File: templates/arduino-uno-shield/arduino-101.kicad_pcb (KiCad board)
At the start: 2 copper layers, 68.6 x 53.3 mm, 8 parts, among them P1 POWER, P2 ANALOG, P3 DIGITAL, P4 DIGITAL, P5 CONN_1, P6 CONN_1, P7 CONN_1, P8 CONN_1

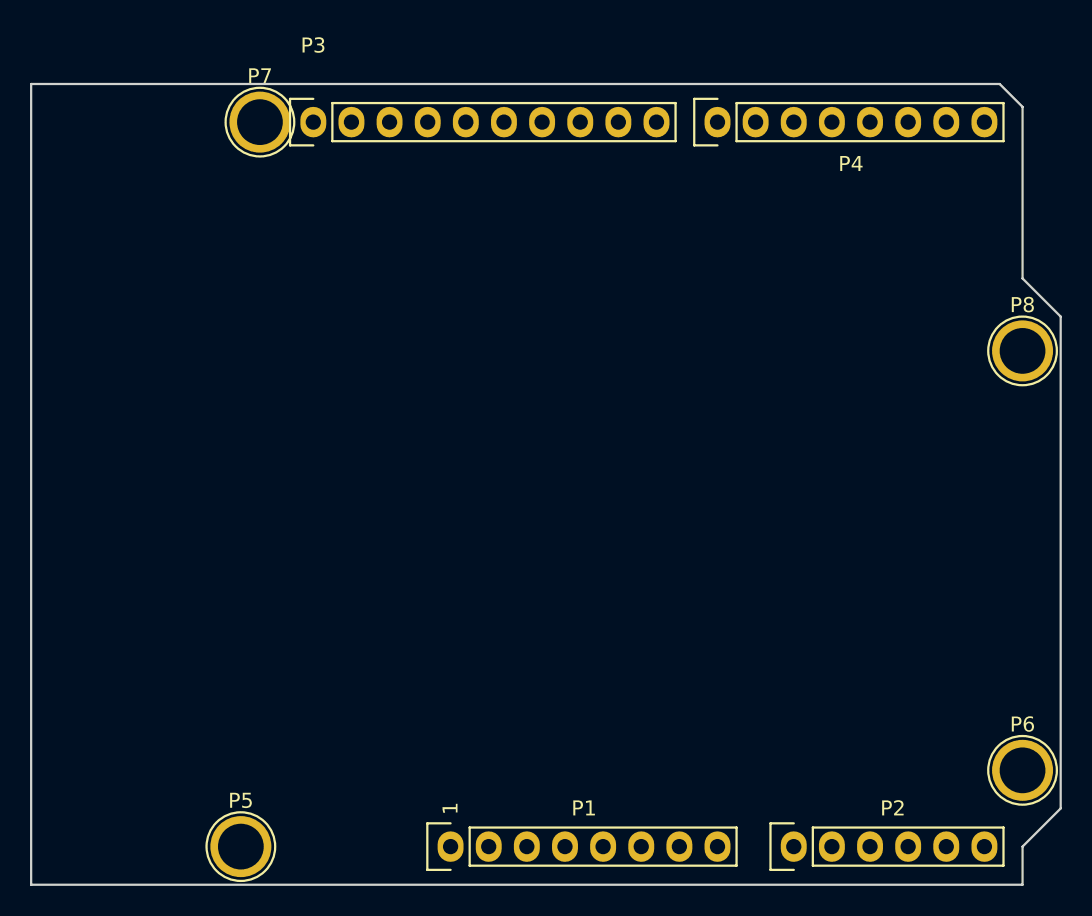
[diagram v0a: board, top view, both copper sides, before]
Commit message: Added complete Arduino 101 template with wickerlib features. Ready for use.
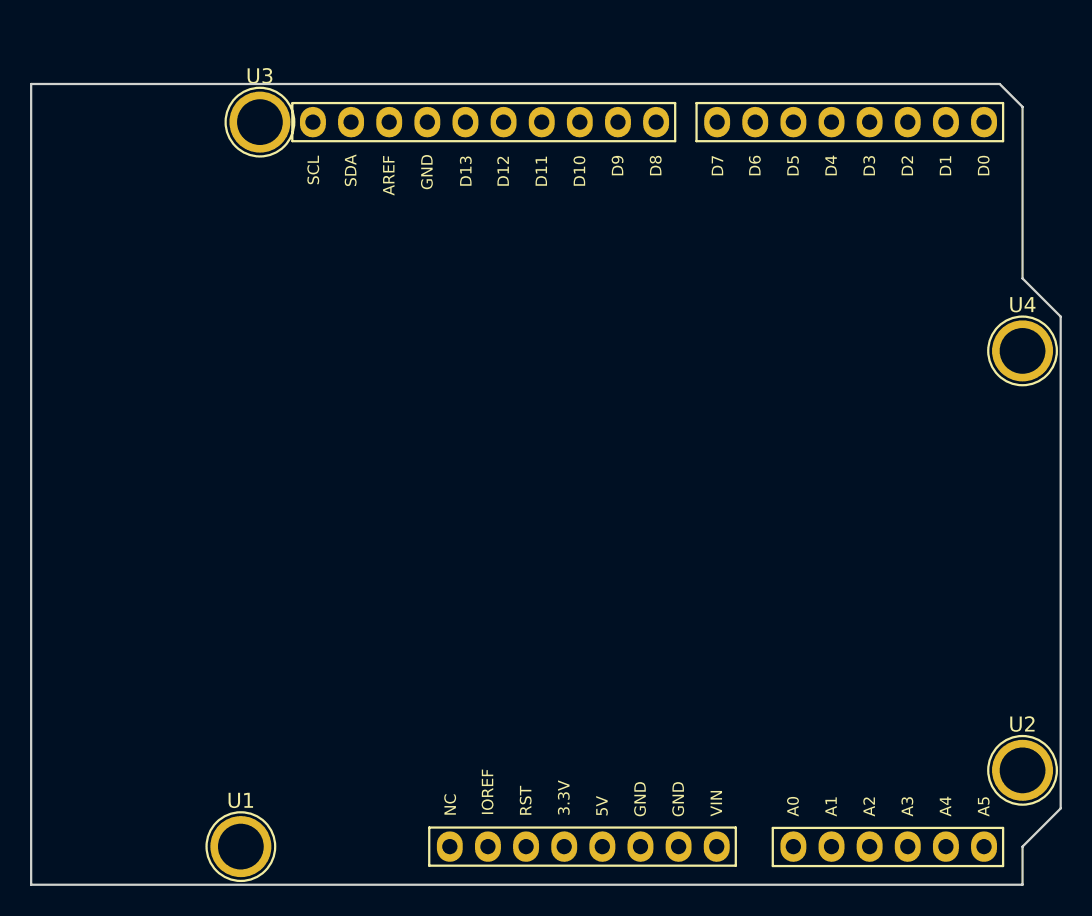
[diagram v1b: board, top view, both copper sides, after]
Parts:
- removed P1: POWER, Socket_Arduino_Uno:Socket_Strip_Arduino_1x08
- removed P2: ANALOG, Socket_Arduino_Uno:Socket_Strip_Arduino_1x06
- removed P3: DIGITAL, Socket_Arduino_Uno:Socket_Strip_Arduino_1x10
- removed P4: DIGITAL, Socket_Arduino_Uno:Socket_Strip_Arduino_1x08
- removed P5, P6, P7, P8: CONN_1, Socket_Arduino_Uno:Arduino_1pin
- added U1: HOLE, Wickerlib:ARDUINO-MOUNTING-HOLE, F.Cu at (125.0, 123.8)
- added U2: HOLE, Wickerlib:ARDUINO-MOUNTING-HOLE, F.Cu at (177.0, 118.7)
- added U3: HOLE, Wickerlib:ARDUINO-MOUNTING-HOLE, F.Cu at (126.2, 75.6)
- added U4: HOLE, Wickerlib:ARDUINO-MOUNTING-HOLE, F.Cu at (177.0, 90.8)
- added U5: ARDUINO-101-SHIELD, Wickerlib:ARDUINO-101-SHIELD, F.Cu at (133.8, 123.8)
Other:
- board text removed: "1"
